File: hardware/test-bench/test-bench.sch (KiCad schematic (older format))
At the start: 44 parts, among them J1 Conn_Mem_Ext, J2 Conn_Reg, J3 SWD, J4 Conn_Mem, J5 FTDI, J6 Conn_Power, J7 J_LINK_SWD, SW1 SW_Push_4pin, SW2 SW_Push_4pin, U1 STM32G030F6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

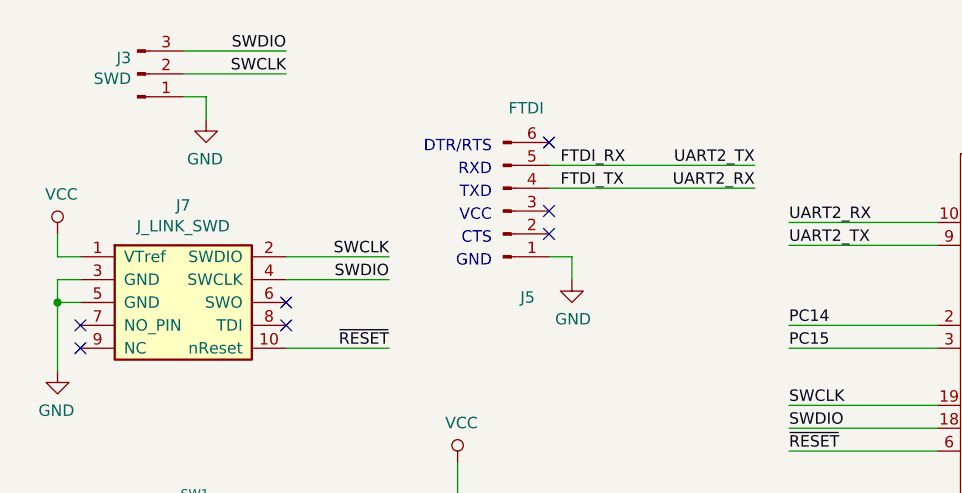
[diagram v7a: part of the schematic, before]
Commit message: Added warning about switched SWDIO and SWCLK to schematic
Should be fixed in rev B
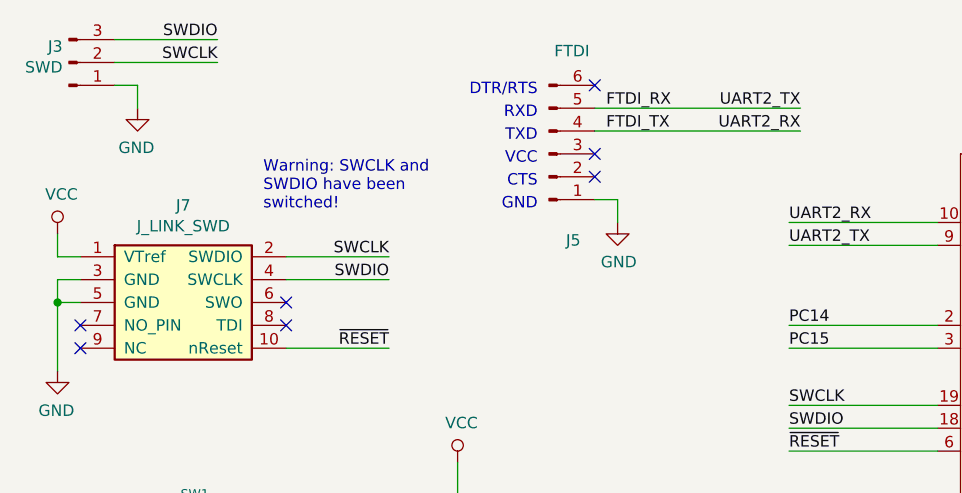
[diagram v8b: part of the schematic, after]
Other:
- note added: "Warning: SWCLK and\nSWDIO have been\nswitched!"
- moved on the sheet: J3, J5
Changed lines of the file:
@@
 L Connector:Conn_01x03_Male J3
 U 1 1 5F42A36C
-P 1000 900
-F 0 "J3" H 972 830 50  0000 R CNN
-F 1 "SWD" H 972 921 50  0000 R CNN
-F 2 "Connector_PinHeader_2.54mm:PinHeader_1x03_P2.54mm_Vertical" H 1000 900 50  0001 C CNN
-F 3 "~" H 1000 900 50  0001 C CNN
-	1    1000 900
+P 700 850
+F 0 "J3" H 672 780 50  0000 R CNN
+F 1 "SWD" H 672 871 50  0000 R CNN
+F 2 "Connector_PinHeader_2.54mm:PinHeader_1x03_P2.54mm_Vertical" H 700 850 50  0001 C CNN
+F 3 "~" H 700 850 50  0001 C CNN
+	1    700  850
 	1    0    0    1
 $EndComp
@@
 L power:GND #PWR?
 U 1 1 5F43A491
-P 1300 1100
-F 0 "#PWR?" H 1300 850 50  0001 C CNN
-F 1 "GND" H 1305 927 50  0000 C CNN
-F 2 "" H 1300 1100 50  0001 C CNN
-F 3 "" H 1300 1100 50  0001 C CNN
-	1    1300 1100
+P 1000 1050
+F 0 "#PWR?" H 1000 800 50  0001 C CNN
+F 1 "GND" H 1005 877 50  0000 C CNN
+F 2 "" H 1000 1050 50  0001 C CNN
+F 3 "" H 1000 1050 50  0001 C CNN
+	1    1000 1050
 	-1   0    0    -1
 $EndComp
 Wire Wire Line
-	1300 1000 1300 1100
-Wire Wire Line
-	1200 800  1650 800
-Text Label 1650 800  2    50   ~ 0
+	1000 950  1000 1050
+Wire Wire Line
+	900  750  1350 750
+Text Label 1350 750  2    50   ~ 0
 SWDIO
-Text Label 1650 900  2    50   ~ 0
+Text Label 1350 850  2    50   ~ 0
 SWCLK
 $Comp
 L Connector:Conn_01x06_Male J5
 U 1 1 5F454060
-P 2600 1500
-F 0 "J5" H 2706 1878 50  0000 C CNN
-F 1 "FTDI" H 2700 1050 50  0000 C CNN
-F 2 "Connector_PinHeader_2.54mm:PinHeader_1x06_P2.54mm_Vertical" H 2600 1500 50  0001 C CNN
-F 3 "~" H 2600 1500 50  0001 C CNN
-	1    2600 1500
+P 2800 1250
+F 0 "J5" H 2906 1628 50  0000 C CNN
+F 1 "FTDI" H 2900 800 50  0000 C CNN
+F 2 "Connector_PinHeader_2.54mm:PinHeader_1x06_P2.54mm_Vertical" H 2800 1250 50  0001 C CNN
+F 3 "~" H 2800 1250 50  0001 C CNN
+	1    2800 1250
 	1    0    0    1
 $EndComp
-NoConn ~ 2800 1200
-NoConn ~ 2800 1600
-NoConn ~ 2800 1500
-Text Label 3700 1400 2    50   ~ 0
+NoConn ~ 3000 950
+NoConn ~ 3000 1350
+NoConn ~ 3000 1250
+Text Label 3900 1150 2    50   ~ 0
 UART2_RX
-Text Label 3700 1300 2    50   ~ 0
+Text Label 3900 1050 2    50   ~ 0
 UART2_TX
 $Comp
 L power:GND #PWR?
 U 1 1 5F501B21
-P 2900 1800
-F 0 "#PWR?" H 2900 1550 50  0001 C CNN
-F 1 "GND" H 2905 1627 50  0000 C CNN
-F 2 "" H 2900 1800 50  0001 C CNN
-F 3 "" H 2900 1800 50  0001 C CNN
-	1    2900 1800
-	1    0    0    -1
-$EndComp
-Wire Wire Line
-	2800 1700 2900 1700
-Wire Wire Line
-	2900 1700 2900 1800
+P 3100 1550
+F 0 "#PWR?" H 3100 1300 50  0001 C CNN
+F 1 "GND" H 3105 1377 50  0000 C CNN
+F 2 "" H 3100 1550 50  0001 C CNN
+F 3 "" H 3100 1550 50  0001 C CNN
+	1    3100 1550
+	1    0    0    -1
+$EndComp
+Wire Wire Line
+	3000 1450 3100 1450
+Wire Wire Line
+	3100 1450 3100 1550
 $Comp
 L riscv-serial:Conn_Power J6
@@
 	9300 9450 9300 9350
 Connection ~ 9300 9350
-Text Label 2850 1300 0    50   ~ 0
+Text Label 3050 1050 0    50   ~ 0
 FTDI_RX
-Text Label 2850 1400 0    50   ~ 0
+Text Label 3050 1150 0    50   ~ 0
 FTDI_TX
-Text Notes 2550 1250 2    50   ~ 0
+Text Notes 2750 1000 2    50   ~ 0
 DTR/RTS
-Text Notes 2550 1350 2    50   ~ 0
+Text Notes 2750 1100 2    50   ~ 0
 RXD
-Text Notes 2550 1450 2    50   ~ 0
+Text Notes 2750 1200 2    50   ~ 0
 TXD
-Text Notes 2550 1550 2    50   ~ 0
+Text Notes 2750 1300 2    50   ~ 0
 VCC
-Text Notes 2550 1650 2    50   ~ 0
+Text Notes 2750 1400 2    50   ~ 0
 CTS
-Text Notes 2550 1750 2    50   ~ 0
+Text Notes 2750 1500 2    50   ~ 0
 GND
 Text Label 750  4800 0    50   ~ 0
@@
 	6950 1450 6950 1550
 Wire Wire Line
-	2800 1300 3700 1300
-Wire Wire Line
-	2800 1400 3700 1400
+	3000 1050 3900 1050
+Wire Wire Line
+	3000 1150 3900 1150
 Wire Wire Line
 	15450 4350 14250 4350
@@
 	2100 2100 1650 2100
 Wire Wire Line
-	1200 900  1650 900
-Wire Wire Line
-	1200 1000 1300 1000
+	900  850  1350 850
+Wire Wire Line
+	900  950  1000 950
 $Comp
 L Device:R R3
@@
 	6500 3950 6500 3900
 Connection ~ 6500 3900
+Text Notes 1550 1500 0    50   ~ 0
+Warning: SWCLK and\nSWDIO have been\nswitched!
 $EndSCHEMATC
